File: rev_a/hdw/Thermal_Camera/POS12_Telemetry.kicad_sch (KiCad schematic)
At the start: 7 parts, among them U501 INA219BxDCN, U502 MCP9804

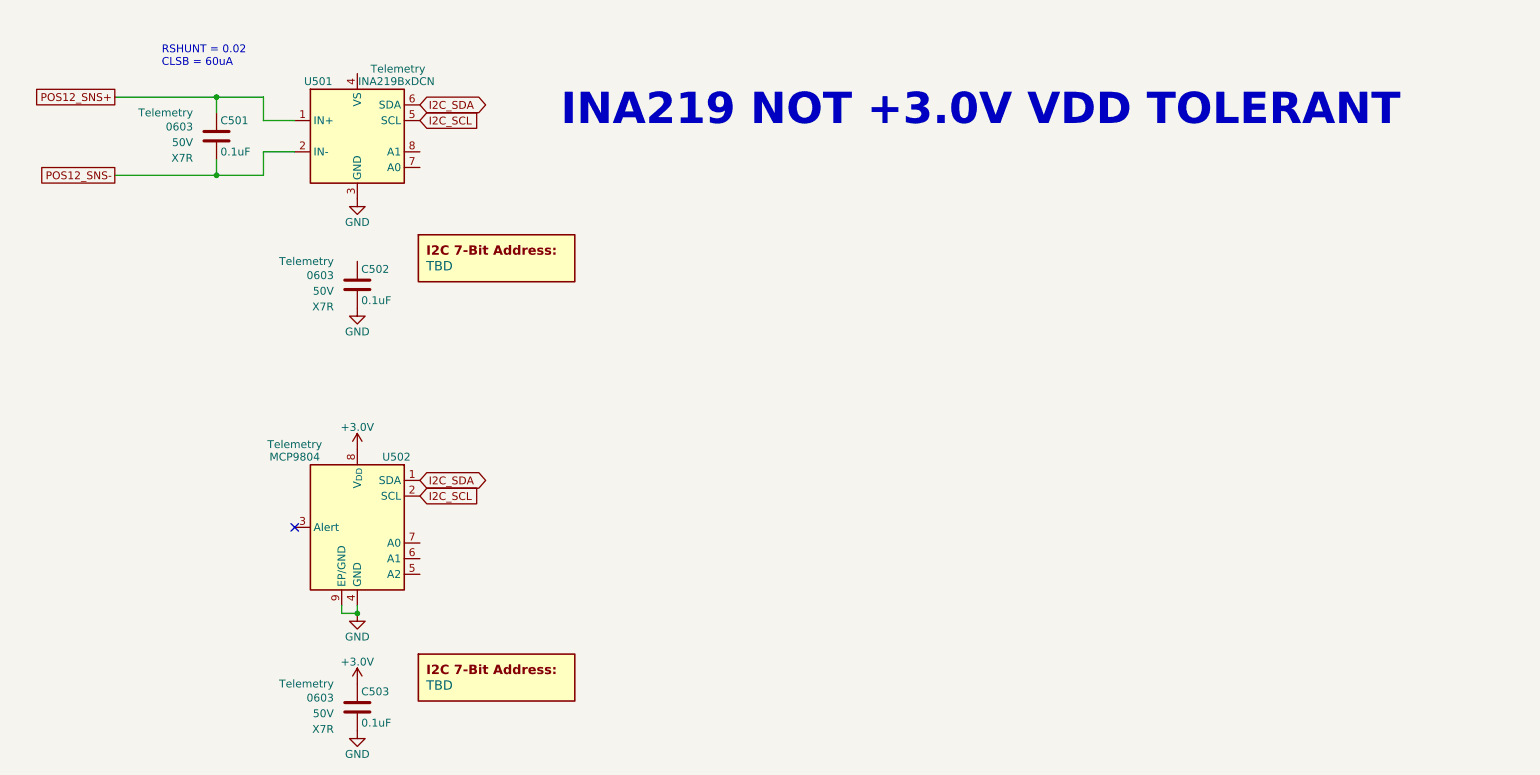
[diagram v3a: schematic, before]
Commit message: added new telemetry circuits
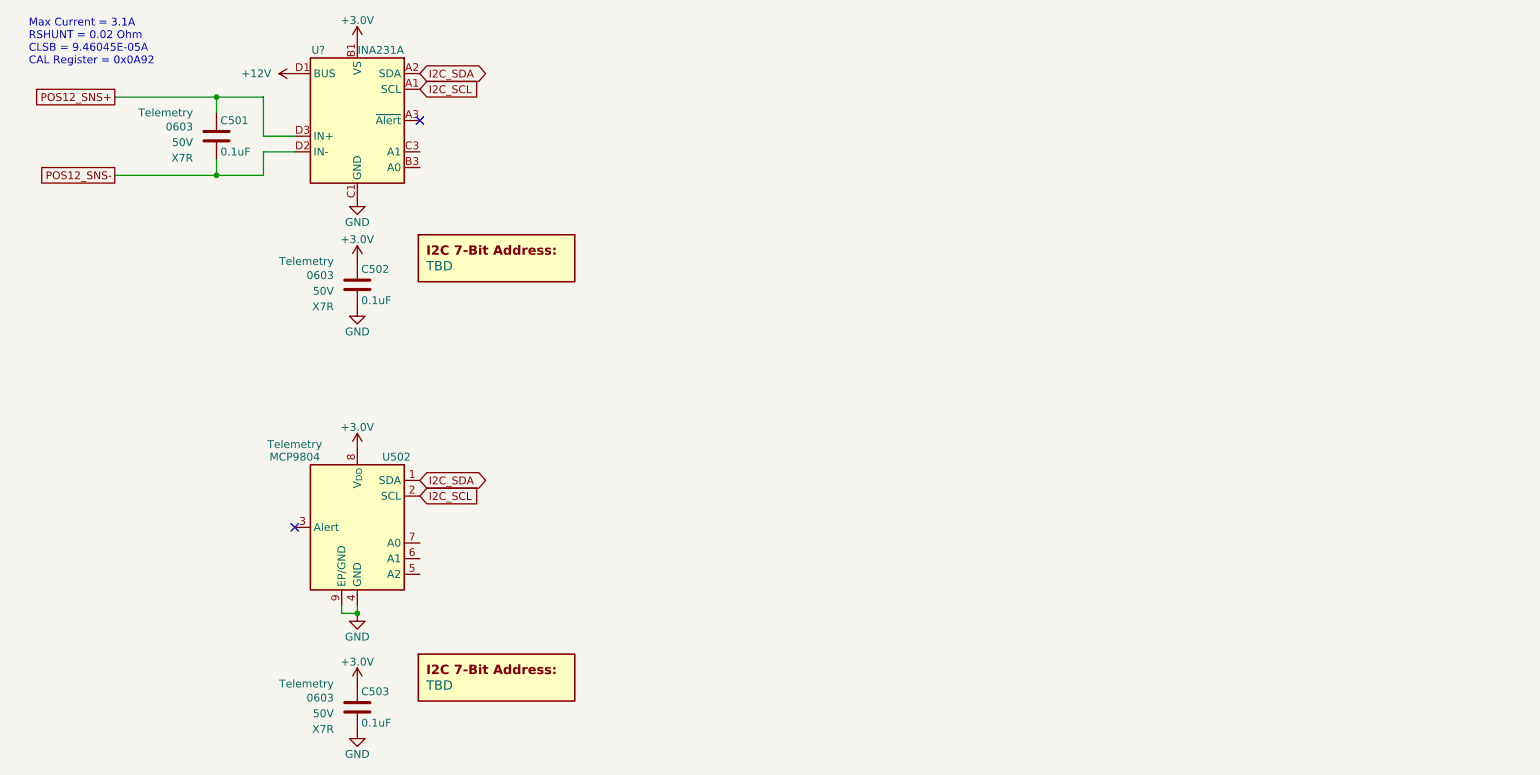
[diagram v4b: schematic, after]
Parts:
- removed U501: INA219BxDCN, Package_TO_SOT_SMD:SOT-23-8, symbol Analog_ADC:INA219BxDCN
- added U?: INA231A, Custom Footprints Library:Texas_DSBGA-12_1.65x1.39mm_Layout3x4_P0.4mm, symbol Custom Library:INA231A
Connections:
- net +3.0V: now also C502.1, U?.B1 (VS)
- net GND: now also U?.C1 (GND)
- net I2C_SCL: now also U?.A1 (SCL)
- net I2C_SDA: now also U?.A2 (SDA)
- net POS12_SNS+: now also U?.D3 (IN+)
- net POS12_SNS-: now also U?.D2 (IN-)
- new net +12V: U?.D1 (BUS)
- no-connect marks 1 -> 2
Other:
- note added: "Max Current = 3.1A RSHUNT = 0.02 Ohm CLSB = 9.46045E-05A CAL Register = 0x0A92"
- note removed: "INA219 NOT +3.0V VDD TOLERANT"
- note removed: "RSHUNT = 0.02 CLSB = 60uA"
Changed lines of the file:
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@@
   (junction (at 113.03 58.42) (diameter 0) (color 0 0 0 0)
   )
+  (no_connect (at 146.05 49.53))
   (no_connect (at 125.73 115.57))
   (wire (pts (xy 96.52 58.42) (xy 113.03 58.42))
@@
     (stroke (width 0) (type default))
   )
-  (wire (pts (xy 125.73 49.53) (xy 120.65 49.53))
-    (stroke (width 0) (type default))
-  )
-  (wire (pts (xy 120.65 49.53) (xy 120.65 45.72))
+  (wire (pts (xy 125.73 52.07) (xy 120.65 52.07))
+    (stroke (width 0) (type default))
+  )
+  (wire (pts (xy 120.65 52.07) (xy 120.65 45.72))
     (stroke (width 0) (type default))
   )
@@
     (stroke (width 0) (type default))
   )
-  (text "RSHUNT = 0.02\nCLSB = 60uA" (at 104.14 40.894 0)
+  (text "Max Current = 3.1A\nRSHUNT = 0.02 Ohm\nCLSB = 9.46045E-05A\nCAL Register = 0x0A92"
+    (at 82.55 40.64 0)
     (effects (font (size 1.27 1.27)) (justify left bottom))
   )
-  (text "INA219 NOT +3.0V VDD TOLERANT" (at 168.91 50.8 0)
-    (effects (font (face "Courier New") (size 5.08 5.08) (thickness 0.508) bold (color 194 0 0 1)) (justify left bottom))
-  )
-  (global_label "I2C_SCL" (shape input) (at 146.05 49.53 0) (fields_autoplaced)
+  (global_label "I2C_SCL" (shape input) (at 146.05 44.45 0) (fields_autoplaced)
     (effects (font (size 1.27 1.27)) (justify left))
-    (property "Intersheetrefs" "${INTERSHEET_REFS}" (at 156.5153 49.53 0)
+    (property "Intersheetrefs" "${INTERSHEET_REFS}" (at 156.5153 44.45 0)
       (effects (font (size 1.27 1.27)) (justify left) hide)
     )
   )
-  (global_label "I2C_SDA" (shape bidirectional) (at 146.05 46.99 0) (fields_autoplaced)
+  (global_label "I2C_SDA" (shape bidirectional) (at 146.05 41.91 0) (fields_autoplaced)
     (effects (font (size 1.27 1.27)) (justify left))
-    (property "Intersheetrefs" "${INTERSHEET_REFS}" (at 157.6871 46.99 0)
+    (property "Intersheetrefs" "${INTERSHEET_REFS}" (at 157.6871 41.91 0)
       (effects (font (size 1.27 1.27)) (justify left) hide)
     )
@@
         (path "/4bd21e0b-5408-4b93-866e-c82ac5b31fa9/78c72208-6db1-4ab8-a8df-528bec958adb"
           (reference "#PWR0302") (unit 1)
+        )
+      )
+    )
+  )
+  (symbol (lib_id "Custom Library:+3.0V") (at 135.89 72.39 0) (unit 1)
+    (in_bom yes) (on_board yes) (dnp no)
+    (property "Reference" "#PWR0303" (at 135.89 76.2 0)
+      (effects (font (size 1.27 1.27)) hide)
+    )
+    (property "Value" "+3.0V" (at 135.89 68.834 0)
+      (effects (font (size 1.27 1.27)))
+    )
+    (property "Footprint" "" (at 135.89 72.39 0)
+      (effects (font (size 1.27 1.27)) hide)
+    )
+    (property "Datasheet" "" (at 135.89 72.39 0)
+      (effects (font (size 1.27 1.27)) hide)
+    )
+    (pin "1")
+    (instances
+      (project "Thermal_Camera"
+        (path "/4bd21e0b-5408-4b93-866e-c82ac5b31fa9/78c72208-6db1-4ab8-a8df-528bec958adb"
+          (reference "#PWR0303") (unit 1)
         )
       )
@@
     )
   )
-  (symbol (lib_id "Analog_ADC:INA219BxDCN") (at 135.89 52.07 0) (unit 1)
-    (in_bom yes) (on_board yes) (dnp no)
-    (property "Reference" "U501" (at 129.54 43.18 0)
-      (effects (font (size 1.27 1.27)))
-    )
-    (property "Value" "INA219BxDCN" (at 142.24 43.18 0)
-      (effects (font (size 1.27 1.27)))
-    )
-    (property "Footprint" "Package_TO_SOT_SMD:SOT-23-8" (at 152.4 60.96 0)
-      (effects (font (size 1.27 1.27)) hide)
-    )
-    (property "Datasheet" "http://www.ti.com/lit/ds/symlink/ina219.pdf" (at 144.78 54.61 0)
-      (effects (font (size 1.27 1.27)) hide)
-    )
-    (property "Digi-Key PN" "296-46420-1-ND" (at 135.89 52.07 0)
-      (effects (font (size 1.27 1.27)) hide)
-    )
-    (property "Configuration" "Telemetry" (at 142.494 41.148 0)
-      (effects (font (size 1.27 1.27)))
-    )
-    (pin "1")
-    (pin "2")
-    (pin "3")
-    (pin "4")
-    (pin "5")
-    (pin "6")
-    (pin "7")
-    (pin "8")
-    (instances
-      (project "Nixie_Clock_Core"
-        (path "/16fdce21-b570-4d81-a458-e8839d611806/9c9d19c1-3649-44f4-8893-4087e4bbe058"
-          (reference "U501") (unit 1)
-        )
-      )
-      (project "LED_Panel_Controller"
-        (path "/22e05ee1-b227-4be7-9418-94433f274720/00000000-0000-0000-0000-00005f581b77"
-          (reference "U?") (unit 1)
-        )
-      )
-      (project "Thermal_Camera"
-        (path "/4bd21e0b-5408-4b93-866e-c82ac5b31fa9/78c72208-6db1-4ab8-a8df-528bec958adb"
-          (reference "U?") (unit 1)
+  (symbol (lib_id "power:+12V") (at 125.73 41.91 90) (unit 1)
+    (in_bom yes) (on_board yes) (dnp no)
+    (property "Reference" "#PWR0301" (at 129.54 41.91 0)
+      (effects (font (size 1.27 1.27)) hide)
+    )
+    (property "Value" "+12V" (at 121.92 41.91 90)
+      (effects (font (size 1.27 1.27)) (justify left))
+    )
+    (property "Footprint" "" (at 125.73 41.91 0)
+      (effects (font (size 1.27 1.27)) hide)
+    )
+    (property "Datasheet" "" (at 125.73 41.91 0)
+      (effects (font (size 1.27 1.27)) hide)
+    )
+    (pin "1")
+    (instances
+      (project "Thermal_Camera"
+        (path "/4bd21e0b-5408-4b93-866e-c82ac5b31fa9/78c72208-6db1-4ab8-a8df-528bec958adb"
+          (reference "#PWR0301") (unit 1)
         )
       )
@@
         )
       )
+    )
+  )
+  (symbol (lib_id "Custom Library:+3.0V") (at 135.89 36.83 0) (unit 1)
+    (in_bom yes) (on_board yes) (dnp no)
+    (property "Reference" "#PWR0309" (at 135.89 40.64 0)
+      (effects (font (size 1.27 1.27)) hide)
+    )
+    (property "Value" "+3.0V" (at 135.89 33.274 0)
+      (effects (font (size 1.27 1.27)))
+    )
+    (property "Footprint" "" (at 135.89 36.83 0)
+      (effects (font (size 1.27 1.27)) hide)
+    )
+    (property "Datasheet" "" (at 135.89 36.83 0)
+      (effects (font (size 1.27 1.27)) hide)
+    )
+    (pin "1")
+    (instances
+      (project "Thermal_Camera"
+        (path "/4bd21e0b-5408-4b93-866e-c82ac5b31fa9/78c72208-6db1-4ab8-a8df-528bec958adb"
+          (reference "#PWR0309") (unit 1)
+        )
+      )
+    )
+  )
+  (symbol (lib_id "Custom Library:INA231A") (at 135.89 49.53 0) (unit 1)
+    (in_bom yes) (on_board yes) (dnp no)
+    (property "Reference" "U?" (at 129.54 38.1 0)
+      (effects (font (size 1.27 1.27)))
+    )
+    (property "Value" "INA231A" (at 139.7 38.1 0)
+      (effects (font (size 1.27 1.27)))
+    )
+    (property "Footprint" "Custom Footprints Library:Texas_DSBGA-12_1.65x1.39mm_Layout3x4_P0.4mm" (at 156.21 60.96 0)
+      (effects (font (size 1.27 1.27)) hide)
+    )
+    (property "Datasheet" "http://www.ti.com/lit/ds/symlink/ina231.pdf" (at 144.78 52.07 0)
+      (effects (font (size 1.27 1.27)) hide)
+    )
+    (property "Digi-Key PN" "296-41263-1-ND" (at 135.89 49.53 0)
+      (effects (font (size 1.27 1.27)) hide)
+    )
+    (pin "B1")
+    (pin "C2")
+    (pin "A1")
+    (pin "A2")
+    (pin "A3")
+    (pin "B3")
+    (pin "C1")
+    (pin "C3")
+    (pin "B2")
+    (pin "D2")
+    (pin "D3")
+    (pin "D1")
+    (instances
+      (project "Thermal_Camera"
+        (path "/4bd21e0b-5408-4b93-866e-c82ac5b31fa9/78c72208-6db1-4ab8-a8df-528bec958adb"
+          (reference "U?") (unit 1)
+        )
+      )

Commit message: lots of schematic progress
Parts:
- C?: renamed from C503; footprint Capacitors_SMD:C_0603 -> (none); Digi-Key PN 1276-1935-1-ND -> (none); display_footprint 0603 -> (none)
- C?: renamed from C501; footprint Capacitors_SMD:C_0603 -> (none); Digi-Key PN 1276-1935-1-ND -> (none); display_footprint 0603 -> (none)
- C?: renamed from C502; footprint Capacitors_SMD:C_0603 -> (none); Digi-Key PN 1276-1935-1-ND -> (none); display_footprint 0603 -> (none)
- DOC?: renamed from DOC501; value TBD -> 0x70
- DOC?: renamed from DOC502; value TBD -> 0x18
- gave numbers to parts that had none: 1
- renumbered U502 to U?
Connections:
- net GND: now also U301.B3 (A0), U301.C3 (A1), U?.5 (A2), U?.6 (A1), U?.7 (A0)
